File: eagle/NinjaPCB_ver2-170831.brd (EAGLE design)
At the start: 72 x 79 mm, 76 parts, among them IC2 VNH5019/VNH3SP30-BNC, IC3 ANALOGSW_AD_SOT23-6NC, IC4 ANALOGSW_TI-SC70-5/6NC, IC5 MCP3551SNNC, IC6 NAU7802NC, J2 ATX24, J3 HEATER, J4 HEATER_TEMP, J5 PELTIER, Q2 IRF520NPBF, Q3 IRF520NPBF, U1 CJT1117-3.3-SOT223

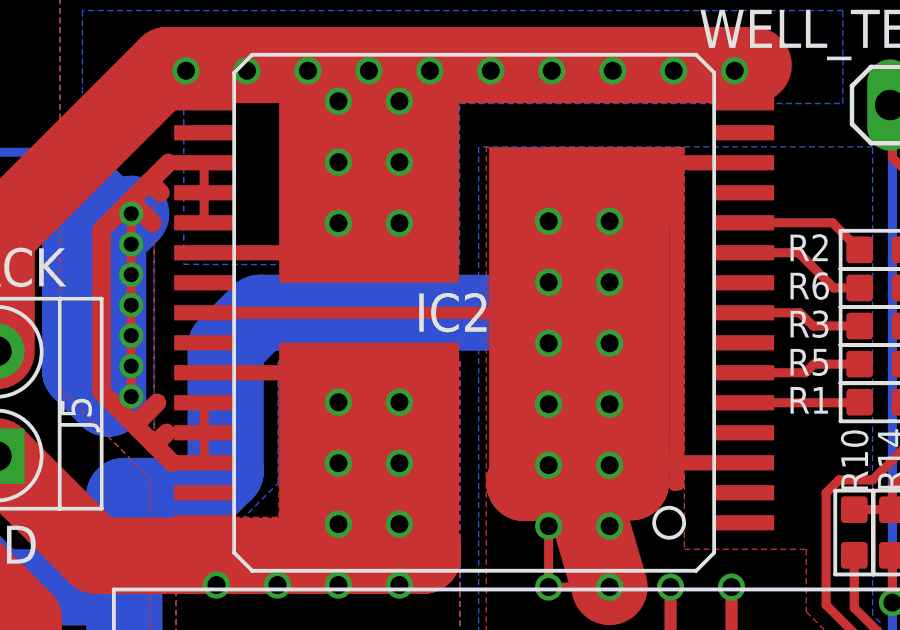
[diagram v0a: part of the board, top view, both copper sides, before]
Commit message: remove ver2 temporary. it will be back after evaluation.
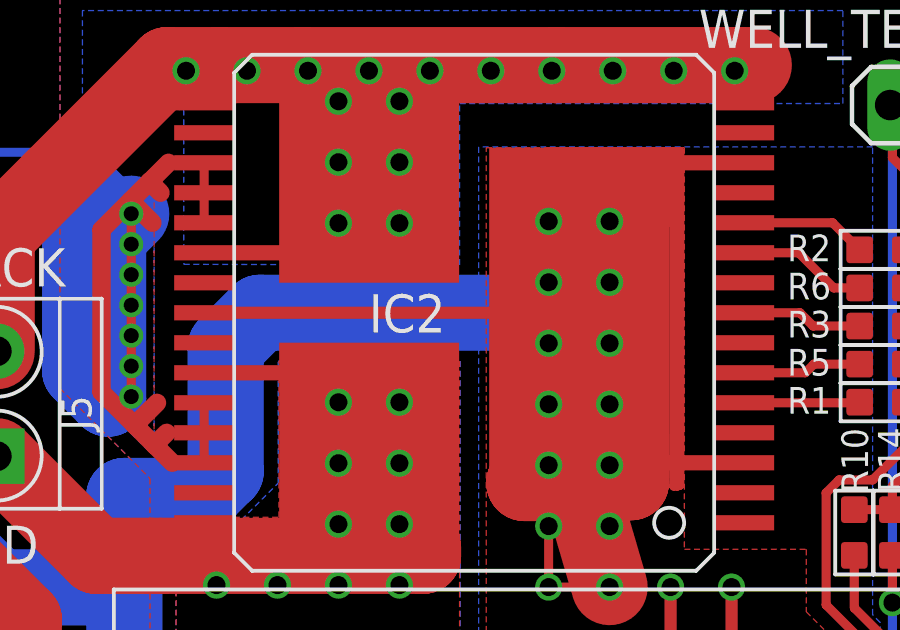
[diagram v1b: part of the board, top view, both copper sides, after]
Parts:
- C8: value CAP_E5-13-L3030RINV -> 3300uF
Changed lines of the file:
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@@
 <attribute name="VALUE" x="54.125" y="-17.8395" size="0.02" layer="27" rot="R90"/>
 </element>
-<element name="C8" library="PCR-RCL" package="E5-13-L30R-INV" value="CAP_E5-13-L3030RINV" x="13.7946" y="-26.2026" smashed="yes" rot="R270">
+<element name="C8" library="PCR-RCL" package="E5-13-L30R-INV" value="3300uF" x="13.7946" y="-26.2026" smashed="yes" rot="R270">
 <attribute name="NAME" x="17.137" y="-32.0634" size="1.778" layer="25" ratio="10"/>
 </element>
@@
 </element>
 <element name="IC2" library="st-microelectronics" package="MULTIPOWERSO-30-B-NOCREAM" value="VNH5019/VNH3SP30-BNC" x="28.806" y="-10.48" smashed="yes" rot="R90">
-<attribute name="NAME" x="26.82" y="-11.11" size="1.27" layer="25"/>
+<attribute name="NAME" x="25.296" y="-11.1354" size="1.27" layer="25"/>
 </element>
 <element name="U$1" library="adafruit" package="PJ-102A" value="2.1MMJACKTHM" x="-0.5" y="-5" rot="R90"/>

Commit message: VNH5019 doesnot have same pinout as VNH3SP30
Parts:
- IC2: value VNH5019/VNH3SP30-BNC -> VNH3SP30-BNC
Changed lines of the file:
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@@
 <attribute name="VALUE" x="65.555" y="-17.8395" size="0.02" layer="27" rot="R90"/>
 </element>
-<element name="IC2" library="st-microelectronics" package="MULTIPOWERSO-30-B-NOCREAM" value="VNH5019/VNH3SP30-BNC" x="28.806" y="-10.48" smashed="yes" rot="R90">
+<element name="IC2" library="st-microelectronics" package="MULTIPOWERSO-30-B-NOCREAM" value="VNH3SP30-BNC" x="28.806" y="-10.48" smashed="yes" rot="R90">
 <attribute name="NAME" x="25.296" y="-11.1354" size="1.27" layer="25"/>
 </element>
